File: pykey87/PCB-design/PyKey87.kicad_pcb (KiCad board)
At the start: 2 copper layers, 352.5 x 120 mm, 310 parts, among them J1 USB_C_Receptacle_USB2.0, J2 Conn_01x03, J3 Conn_01x04, J4 AudioJack4, J5 Conn_01x04, SW1 SW_SPST, SW2 SW_SPDT, U1 CherryMX_LTST-A683CEGBW, U10 CherryMX_LTST-A683CEGBW, U100 RP2040, U101 USBLC6-2SC6, U102 W25Q128JVS, U103 AMS1117-3.3, U11 CherryMX_LTST-A683CEGBW, U12 CherryMX_LTST-A683CEGBW, U13 CherryMX_LTST-A683CEGBW, U14 CherryMX_LTST-A683CEGBW, U15 CherryMX_LTST-A683CEGBW, U16 CherryMX_LTST-A683CEGBW, U17 CherryMX_LTST-A683CEGBW, U18 CherryMX_LTST-A683CEGBW, U19 CherryMX_LTST-A683CEGBW, U2 CherryMX_LTST-A683CEGBW, U20 CherryMX_LTST-A683CEGBW, U21 CherryMX_LTST-A683CEGBW, U22 CherryMX_LTST-A683CEGBW, U23 CherryMX_LTST-A683CEGBW, U24 CherryMX_LTST-A683CEGBW, U25 CherryMX_LTST-A683CEGBW, U26 CherryMX_LTST-A683CEGBW, U27 CherryMX_LTST-A683CEGBW, U28 CherryMX_LTST-A683CEGBW, U29 CherryMX_LTST-A683CEGBW, U3 CherryMX_LTST-A683CEGBW, U30 CherryMX_LTST-A683CEGBW, U31 CherryMX_LTST-A683CEGBW, U32 CherryMX_LTST-A683CEGBW, U33 CherryMX_LTST-A683CEGBW, U34 CherryMX_LTST-A683CEGBW, U35 CherryMX_LTST-A683CEGBW, U36 CherryMX_LTST-A683CEGBW, U37 CherryMX_LTST-A683CEGBW, U38 CherryMX_LTST-A683CEGBW, U39 CherryMX_LTST-A683CEGBW, U4 CherryMX_LTST-A683CEGBW, U40 CherryMX_LTST-A683CEGBW, U41 CherryMX_LTST-A683CEGBW, U42 CherryMX_LTST-A683CEGBW, U43 CherryMX_LTST-A683CEGBW, U44 CherryMX_LTST-A683CEGBW, U45 CherryMX_LTST-A683CEGBW, U46 CherryMX_LTST-A683CEGBW, U47 CherryMX_LTST-A683CEGBW, U48 CherryMX_LTST-A683CEGBW, U49 CherryMX_LTST-A683CEGBW, U5 CherryMX_LTST-A683CEGBW, U50 CherryMX_LTST-A683CEGBW, U51 CherryMX_LTST-A683CEGBW, U52 CherryMX_LTST-A683CEGBW, U53 CherryMX_LTST-A683CEGBW, U54 CherryMX_LTST-A683CEGBW, U55 CherryMX_LTST-A683CEGBW, U56 CherryMX_LTST-A683CEGBW, U57 CherryMX_LTST-A683CEGBW, U58 CherryMX_LTST-A683CEGBW, U59 CherryMX_LTST-A683CEGBW, U6 CherryMX_LTST-A683CEGBW, U60 CherryMX_LTST-A683CEGBW, U61 CherryMX_LTST-A683CEGBW, U62 CherryMX_LTST-A683CEGBW, U63 CherryMX_LTST-A683CEGBW, U64 CherryMX_LTST-A683CEGBW, U65 CherryMX_LTST-A683CEGBW, U66 CherryMX_LTST-A683CEGBW, U67 CherryMX_LTST-A683CEGBW, U68 CherryMX_LTST-A683CEGBW, U69 CherryMX_LTST-A683CEGBW, U7 CherryMX_LTST-A683CEGBW, U70 CherryMX_LTST-A683CEGBW, U71 CherryMX_LTST-A683CEGBW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

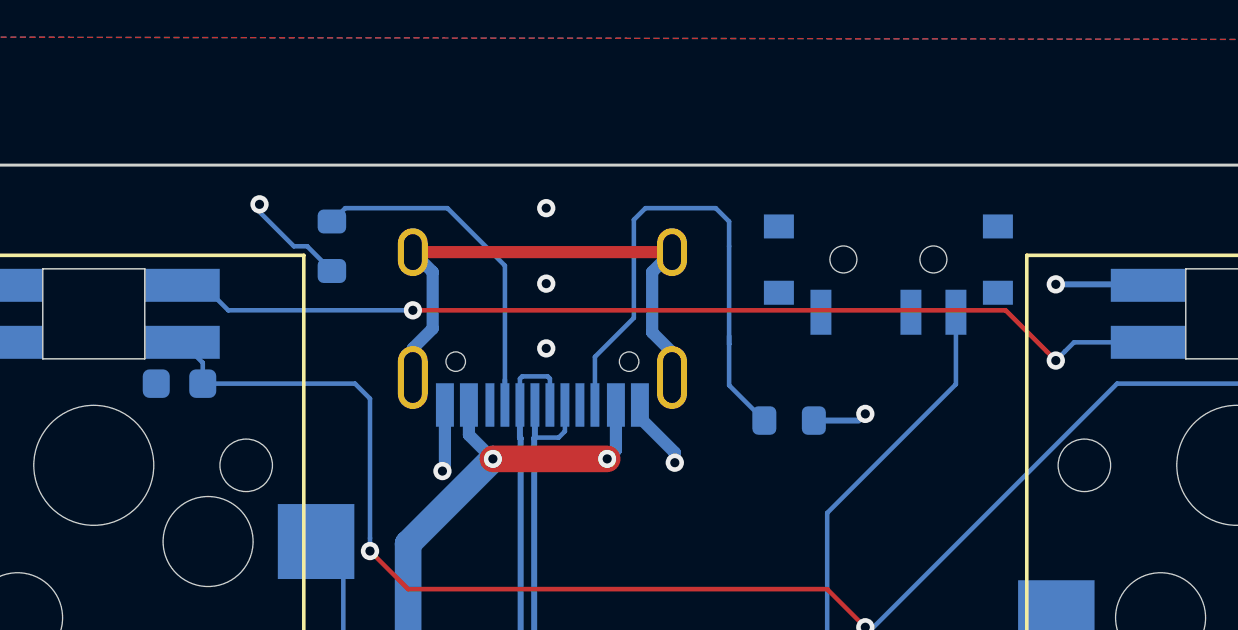
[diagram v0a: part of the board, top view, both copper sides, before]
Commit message: Moved R1 and R2 further from USB
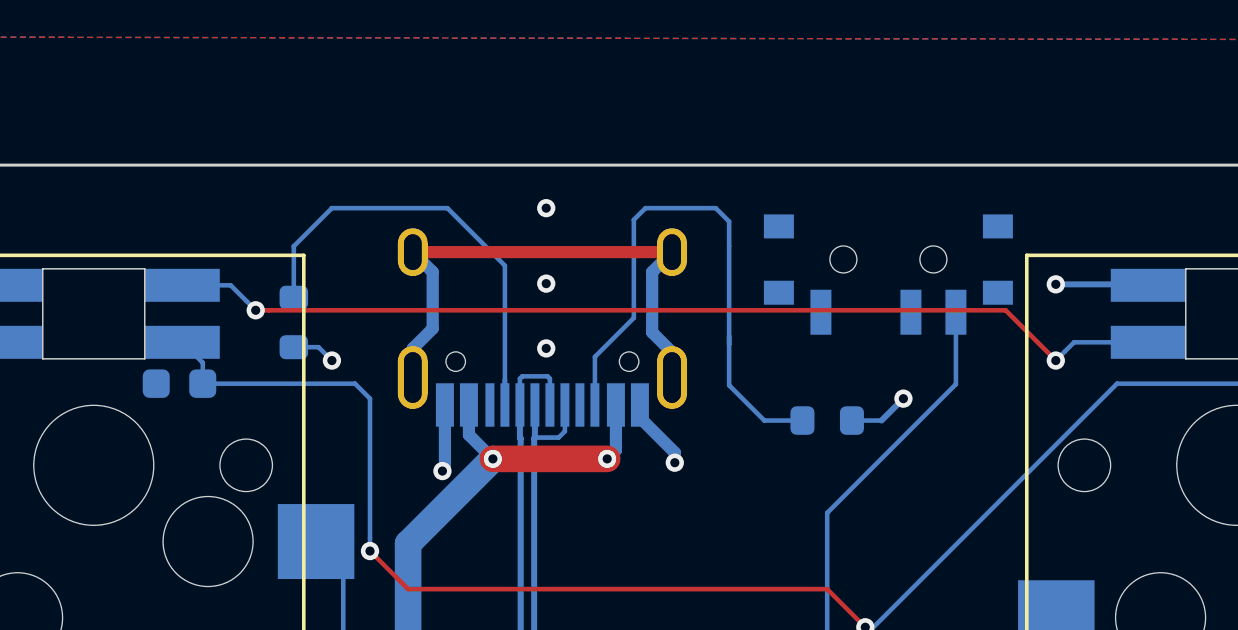
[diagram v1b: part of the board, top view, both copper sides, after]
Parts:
- moved R1 2.84 mm to (78.1, 45.2)
- moved R2 1.27 mm to (95.9, 48.5)
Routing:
- net Net-(J1-PadA5): track 12.2 -> 15.6 mm
- net GND: track 289.2 -> 287.7 mm
- net Net-(J1-PadB5): track 17.6 -> 18.9 mm
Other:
- board text added: "CERN-OHL-W 2021-11-17 - Pierre Constantineau & nitronarcosis"
- board text removed: "CERN-OHL-W 2021-11-15 - Pierre Constantineau & nitronarcosis"
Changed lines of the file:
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@@
     (thickness 1.6002)
     (drawings 94)
-    (tracks 3949)
+    (tracks 3950)
     (zones 0)
     (modules 310)
@@
     (tags SOD-123)
     (attr smd)
-    (fp_text reference D87 (at 0 -1.87 90) (layer B.SilkS)
+    (fp_text reference D87 (at 1.07 1.94 90) (layer B.SilkS)
       (effects (font (size 1 1) (thickness 0.15)) (justify mirror))
     )
@@
     (tags SOD-123)
     (attr smd)
-    (fp_text reference D86 (at -1.27 -1.87 90) (layer B.SilkS)
+    (fp_text reference D86 (at 0 -1.87 90) (layer B.SilkS)
       (effects (font (size 1 1) (thickness 0.15)) (justify mirror))
     )
@@
   )
   (module Resistor_SMD:R_0603_1608Metric (layer Back)
-    (at 79.375 42.705 90)
+    (at 78.105 45.245 90)
     (descr "Resistor SMD 0603 (1608 Metric), square (rectangular) end terminal, IPC_7351 nominal, (Body size source: IPC-SM-782 page 72, https://www.pcb-3d.com/wordpress/wp-content/uploads/ipc-sm-782a_amendment_1_and_2.pdf), generated with kicad-footprint-generator")
     (tags resistor)
@@
   )
   (module Resistor_SMD:R_0603_1608Metric (layer Back)
-    (at 94.615 48.515 180)
+    (at 95.885 48.515 180)
     (descr "Resistor SMD 0603 (1608 Metric), square (rectangular) end terminal, IPC_7351 nominal, (Body size source: IPC-SM-782 page 72, https://www.pcb-3d.com/wordpress/wp-content/uploads/ipc-sm-782a_amendment_1_and_2.pdf), generated with kicad-footprint-generator")
     (tags resistor)
@@
   )
   (gr_text "SDA\nSCL\n+3V3\nGND" (at 365.125 111.285) (layer B.SilkS)
-    (effects (font (size 1.5 1.524) (thickness 0.3048)) (justify mirror))
+    (effects (font (size 1.524 1.524) (thickness 0.3048)) (justify mirror))
   )
   (gr_text Reset (at 173.355 41.435 180) (layer B.SilkS)
@@
   )
   (gr_text Qwiic (at 250.825 146.845) (layer B.SilkS)
-    (effects (font (size 2.032 1.524) (thickness 0.3048)) (justify mirror))
+    (effects (font (size 1 1) (thickness 0.15)) (justify mirror))
   )
   (gr_arc (start 410 42) (end 410 40) (angle 90) (layer Edge.Cuts) (width 0.1))
@@
     (effects (font (size 1 1) (thickness 0.1)) (justify mirror))
   )
-  (gr_text "    CERN-OHL-W\n2021-11-15 - Pierre Constantineau & nitronarcosis" (at 310.594 140.495) (layer B.SilkS)
+  (gr_text "    CERN-OHL-W\n2021-11-17 - Pierre Constantineau & nitronarcosis" (at 310.594 140.495) (layer B.SilkS)
     (effects (font (size 1.524 1.524) (thickness 0.3048)) (justify left mirror))
   )
@@
   (via (at 159.766 143.67) (size 0.6096) (drill 0.3048) (layers Front Back) (net 61))
   (segment (start 161.207 143.67) (end 159.766 143.67) (width 0.1524) (layer Back) (net 61) (status 10))
-  (via (at 76.962 41.308) (size 0.6096) (drill 0.3048) (layers Front Back) (net 61))
   (via (at 167.259 138.844) (size 0.6096) (drill 0.3048) (layers Front Back) (net 61))
   (via (at 170.658344 138.6915) (size 0.6096) (drill 0.3048) (layers Front Back) (net 61))
@@
   (segment (start 106.555 43.975) (end 106.5875 44.0075) (width 0.2) (layer Back) (net 61))
   (segment (start 103.505 43.975) (end 106.555 43.975) (width 0.2) (layer Back) (net 61))
-  (via (at 97.155002 48.292987) (size 0.6096) (drill 0.3048) (layers Front Back) (net 61))
-  (segment (start 95.44 48.515) (end 96.932989 48.515) (width 0.2) (layer Back) (net 61))
   (segment (start 98.675 44.905) (end 98.675 45.305) (width 0.2) (layer Back) (net 61))
   (via (at 79.375 121.445) (size 0.6096) (drill 0.3048) (layers Front Back) (net 61))
@@
   (via (at 186.055 107.475) (size 0.6096) (drill 0.3048) (layers Front Back) (net 61))
   (via (at 125.095 135.415) (size 0.6096) (drill 0.3048) (layers Front Back) (net 61))
-  (segment (start 78.55 42.705) (end 79.375 43.53) (width 0.1524) (layer Back) (net 61))
-  (segment (start 78.105 42.705) (end 78.55 42.705) (width 0.1524) (layer Back) (net 61))
-  (segment (start 76.962 41.308) (end 76.962 41.562) (width 0.1524) (layer Back) (net 61))
-  (segment (start 76.962 41.562) (end 78.105 42.705) (width 0.1524) (layer Back) (net 61))
   (via (at 180.975 47.785) (size 0.6096) (drill 0.3048) (layers Front Back) (net 61))
   (via (at 90.805 49.92) (size 0.6096) (drill 0.3048) (layers Front Back) (net 61))
@@
   (via (at 260.985 85.885) (size 0.6096) (drill 0.3048) (layers Front Back) (net 61))
   (via (at 84.455 70.645) (size 0.6096) (drill 0.3048) (layers Front Back) (net 61))
+  (via (at 79.375 46.515) (size 0.6096) (drill 0.3048) (layers Front Back) (net 61))
+  (segment (start 78.105 46.07) (end 78.93 46.07) (width 0.1524) (layer Back) (net 61))
+  (segment (start 78.93 46.07) (end 79.375 46.515) (width 0.1524) (layer Back) (net 61))
+  (via (at 98.425 47.785) (size 0.6096) (drill 0.3048) (layers Front Back) (net 61))
+  (segment (start 97.695 48.515) (end 98.425 47.785) (width 0.2) (layer Back) (net 61))
+  (segment (start 96.71 48.515) (end 97.695 48.515) (width 0.1524) (layer Back) (net 61))
   (segment (start 97.928 125.763) (end 95.275 128.416) (width 0.889) (layer Back) (net 62) (status 20))
   (segment (start 98.399 125.763) (end 97.928 125.763) (width 0.889) (layer Back) (net 62) (status 10))
@@
   (segment (start 84.455 85.885) (end 87.9314 85.885) (width 0.4064) (layer Back) (net 62))
   (segment (start 85.142 47.996) (end 85.142 47.146) (width 0.1524) (layer Back) (net 63))
-  (segment (start 79.82 41.435) (end 79.375 41.88) (width 0.1524) (layer Back) (net 63))
-  (segment (start 83.225 41.435) (end 79.82 41.435) (width 0.1524) (layer Back) (net 63))
+  (segment (start 78.105 42.705) (end 78.105 44.42) (width 0.1524) (layer Back) (net 63))
+  (segment (start 79.375 41.435) (end 78.105 42.705) (width 0.1524) (layer Back) (net 63))
+  (segment (start 83.225 41.435) (end 79.375 41.435) (width 0.1524) (layer Back) (net 63))
   (segment (start 85.142 47.996) (end 85.142 43.352) (width 0.1524) (layer Back) (net 63))
   (segment (start 85.142 43.352) (end 83.225 41.435) (width 0.1524) (layer Back) (net 63))
@@
   (segment (start 92.615 45.69) (end 92.615 45.975) (width 0.1524) (layer Back) (net 64))
   (segment (start 92.615 45.975) (end 92.615 47.34) (width 0.1524) (layer Back) (net 64))
+  (segment (start 93.79 48.515) (end 95.06 48.515) (width 0.1524) (layer Back) (net 64))
   (segment (start 145.8602 149.131) (end 156.846 149.131) (width 0.2) (layer Back) (net 65))
   (segment (start 136.765432 140.036232) (end 145.8602 149.131) (width 0.2) (layer Back) (net 65))
@@
   (via (at 158.115 157.005) (size 0.6096) (drill 0.3048) (layers Front Back) (net 222))
   (segment (start 155.0925 155.735) (end 156.3625 157.005) (width 0.1524) (layer Back) (net 222))
-  (via (at 82.074 44.84) (size 0.6096) (drill 0.3048) (layers Front Back) (net 223))
-  (segment (start 75.0875 44.0075) (end 74.3875 44.0075) (width 0.1524) (layer Back) (net 223))
-  (segment (start 75.92 44.84) (end 75.0875 44.0075) (width 0.1524) (layer Back) (net 223))
-  (segment (start 82.074 44.84) (end 75.92 44.84) (width 0.1524) (layer Back) (net 223))
   (segment (start 103.809799 46.210201) (end 103.505 46.515) (width 0.1524) (layer Back) (net 223))
   (segment (start 104.1125 45.9075) (end 103.809799 46.210201) (width 0.1524) (layer Back) (net 223))
   (segment (start 106.5875 45.9075) (end 104.1125 45.9075) (width 0.1524) (layer Back) (net 223))
   (via (at 103.505 46.515) (size 0.6096) (drill 0.3048) (layers Front Back) (net 223))
-  (segment (start 103.200201 46.210201) (end 103.505 46.515) (width 0.1524) (layer Front) (net 223))
-  (segment (start 82.074 44.84) (end 101.83 44.84) (width 0.1524) (layer Front) (net 223))
-  (segment (start 101.83 44.84) (end 103.200201 46.210201) (width 0.1524) (layer Front) (net 223))
+  (segment (start 101.83 44.84) (end 77.266052 44.84) (width 0.1524) (layer Front) (net 223))
+  (segment (start 77.266052 44.84) (end 76.835 44.84) (width 0.1524) (layer Front) (net 223))
+  (segment (start 76.530201 44.535201) (end 76.835 44.84) (width 0.1524) (layer Back) (net 223))
+  (segment (start 76.0025 44.0075) (end 76.530201 44.535201) (width 0.1524) (layer Back) (net 223))
+  (segment (start 74.3875 44.0075) (end 76.0025 44.0075) (width 0.1524) (layer Back) (net 223))
+  (segment (start 103.505 46.515) (end 101.83 44.84) (width 0.1524) (layer Front) (net 223))
+  (via (at 76.835 44.84) (size 0.6096) (drill 0.3048) (layers Front Back) (net 223))
   (segment (start 117.54 42.705) (end 116.2375 44.0075) (width 0.1524) (layer Back) (net 224))
   (segment (start 120.015 42.705) (end 117.54 42.705) (width 0.1524) (layer Back) (net 224))

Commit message: Misc fixes to schematic, PCB, and plates
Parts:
- moved D65 2.24 mm to (153.3, 58.7)
- moved D66 2.06 mm to (172.9, 58.7)
- moved D64 2.04 mm to (135.3, 58.7)
- moved D70 2.04 mm to (259.3, 58.7)
- moved D67 2.00 mm to (202.6, 58.7)
- moved D68 2.00 mm to (221.6, 58.7)
- moved D69 2.00 mm to (240.7, 58.7)
- moved D71 2.00 mm to (287.7, 58.7)
- moved D72 2.00 mm to (306.7, 58.7)
- moved D73 2.00 mm to (325.8, 58.7)
- moved D74 2.00 mm to (344.8, 58.7)
- moved D75 2.00 mm to (368.9, 58.7)
- moved D76 2.00 mm to (386.7, 58.7)
- moved D77 2.00 mm to (406.1, 58.7)
- moved D62 1.27 mm to (78.1, 57.9)
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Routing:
- net ROW0: track 567.5 -> 579.1 mm
- net Net-(D76-Pad2): track 4.15 -> 6.69 mm
- net RGBData1: track 372.1 -> 374.0 mm
- net Net-(D77-Pad2): track 4.39 -> 6.27 mm
- net Net-(D64-Pad2): track 4.86 -> 6.54 mm
- net Net-(D75-Pad2): track 4.99 -> 6.63 mm
- net Net-(D73-Pad2): track 4.86 -> 6.50 mm
- net Net-(D71-Pad2): track 4.86 -> 6.50 mm
- net Net-(D69-Pad2): track 5.12 -> 6.77 mm
- net Net-(D74-Pad2): track 4.86 -> 6.50 mm
- net Net-(D68-Pad2): track 5.12 -> 6.77 mm
- net Net-(D67-Pad2): track 5.12 -> 6.77 mm
- net Net-(D72-Pad2): track 4.86 -> 6.50 mm
- net Net-(D70-Pad2): track 5.12 -> 6.61 mm
- net Net-(D66-Pad2): track 4.86 -> 6.30 mm
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
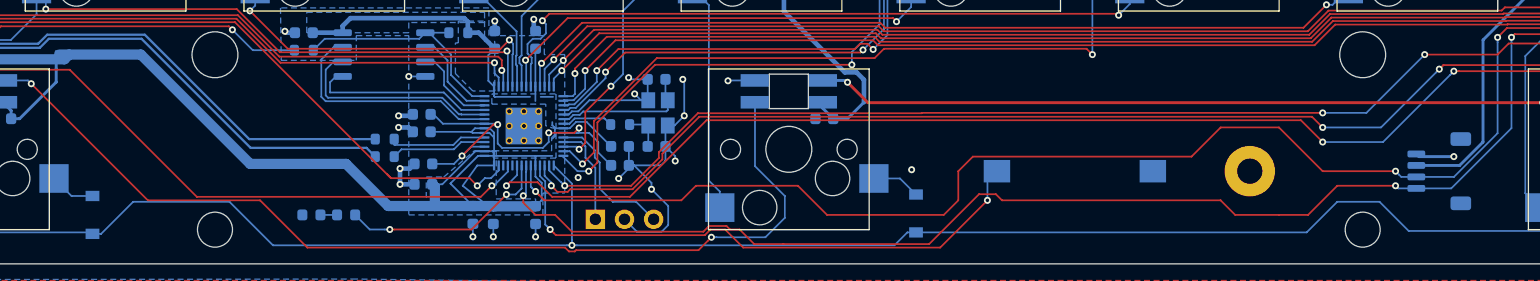
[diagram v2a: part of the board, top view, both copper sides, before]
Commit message: Moved Row0, and rotated stabilizers in plate
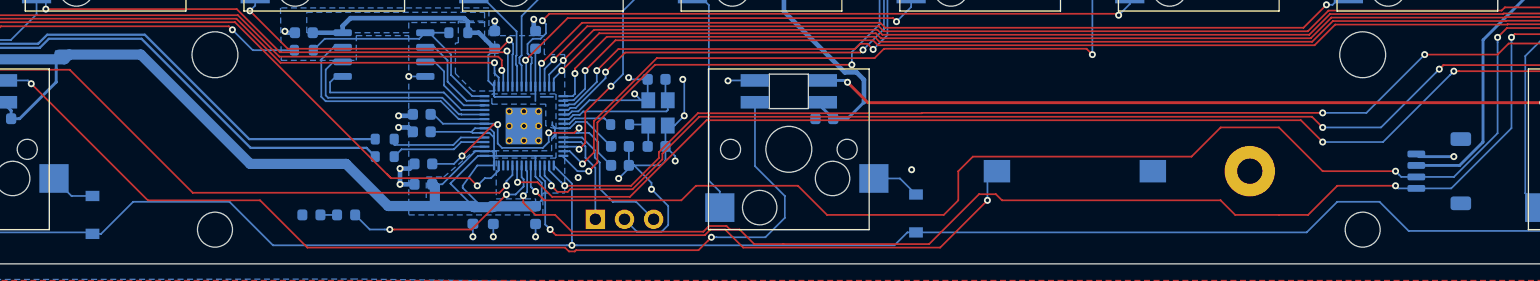
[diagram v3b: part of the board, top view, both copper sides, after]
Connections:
- U100 pad 38: Net-(U100-Pad38) -> ROW0
- U100 pad 39: ROW0 -> Net-(U100-Pad39)
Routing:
- net COL17: track 339.5 -> 337.7 mm
- net ROW0: track 579.1 -> 579.7 mm
